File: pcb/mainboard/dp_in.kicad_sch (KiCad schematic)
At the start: 38 parts, among them J602 Molex_47272_DP, U601 PTN3460

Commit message: pcb: r0p4
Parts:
- removed J602: Molex_47272_DP, footprints:472720024, symbol symbols:Molex_47272_DP
- removed R601: 0, Resistor_SMD:R_0402_1005Metric, symbol Device:R
- removed R603, R604: 4.7K, Resistor_SMD:R_0402_1005Metric, symbol Device:R
- removed R605, R606: 10K, Resistor_SMD:R_0402_1005Metric, symbol Device:R
- removed R607, R608, R609, R610, R611, R612, R613, R614, R615, R616: 100, Resistor_SMD:R_0402_1005Metric, symbol Device:R
- removed TP601, TP602: TestPoint, TestPoint:TestPoint_Pad_D1.0mm, symbol Connector:TestPoint
- added C616, C617, C619, C620, C621, C622: 100nF, Capacitor_SMD:C_0402_1005Metric, symbol Device:C
- added C618: 10uF, Capacitor_SMD:C_0603_1608Metric, symbol Device:C
- added J601: USB_C_Receptacle, Connector_USB:USB_C_Receptacle_Amphenol_12401548E4-2A, symbol Connector:USB_C_Receptacle
- added U602: TPS2001D, Package_TO_SOT_SMD:SOT-23-5, symbol symbols:TPS2001D
- added U603: USBLC6-2P6, Package_TO_SOT_SMD:SOT-666, symbol Power_Protection:USBLC6-2P6
- added U604: FUSB302BMPX, Package_DFN_QFN:WQFN-14-1EP_2.5x2.5mm_P0.5mm_EP1.45x1.45mm, symbol Interface_USB:FUSB302BMPX
- added U605: CBTL02043A, Package_DFN_QFN:WQFN-20-1EP_2.5x4.5mm_P0.5mm_EP1x2.9mm, symbol Analog_Switch:CBTL02043A
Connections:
- net +3V3: now also C619.1, C620.1, U604.12 (VCONN), U604.13 (VCONN), U604.3 (VDD), U604.4 (VDD), U605.1 (VDD), U605.10 (VDD), U605.6 (VDD); no longer R617.1
- net DP0N: now also U605.7 (A1_P); no longer C602.2
- net DP0P: now also U605.8 (A1_N); no longer C601.2
- net DP1N: now also U605.3 (A0_P); no longer C604.2
- net DP1P: now also U605.4 (A0_N); no longer C603.2
- net DPAUXN: now also C622.2; no longer C606.2
- net DPAUXP: now also C621.2; no longer C605.2
- net GND: now also R617.1, C618.1, C619.2, C620.2, J601.A1 (GND), J601.A12 (GND), J601.B1 (GND), J601.B12 (GND), J601.S1 (SHIELD), U602.2 (GND), U603.2 (GND), U604.15 (GND), U604.8 (GND), U604.9 (GND), U605.11 (GND), U605.20 (GND), U605.21 (GND), U605.5 (GND), U605.9 (SEL)
- net I2C_SCL: now also U604.6 (SCL)
- net I2C_SDA: now also U604.7 (SDA)
- net DP_HPD: now reaches U601.11 (HPDRX)
- net DP_VALID: now reaches U601.26 (BKLTEN)
- net AUXN renamed TX2P
- net TX2P: now also J601.A11 (RX2+)
- net AUXP renamed TX2N
- net TX2N: now also J601.A10 (RX2-)
- net D0N renamed TX1P
- net TX1P: now also J601.B11 (RX1+)
- net D0P renamed TX1N
- net TX1N: now also J601.B10 (RX1-)
- net D1N renamed RX1P
- net RX1P: now also J601.A2 (TX1+)
- net D1P renamed RX1N
- net RX1N: now also J601.A3 (TX1-)
- net DDC_SCL: no longer names the net of U601.29 (DDC_SCL)
- net DDC_SDA: no longer names the net of U601.30 (DDC_SDA)
- net LVDS_EVEN_CKN: no longer names the net of U601.35 (LVSCKE_N)
- net LVDS_EVEN_CKP: no longer names the net of U601.34 (LVSCKE_P)
- net LVDS_EVEN_DN: no longer names the net of U601.32 (LVSDE_P)
- net LVDS_EVEN_DP: no longer names the net of U601.31 (LVSDE_N)
- net LVDS_ODD_DN: no longer names the net of U601.44 (LVSDO_N)
- net LVDS_ODD_DP: no longer names the net of U601.43 (LVSDO_P)
- new net +5V: C618.2, U602.1 (OUT)
- new net CC1: J601.A5 (CC1), U604.10 (CC1), U604.11 (CC1)
- new net CC2: J601.B5 (CC2), U604.1 (CC2), U604.14 (CC2)
- new net RX1NC: C603.2, U605.17 (B1_P)
- new net RX1PC: C604.2, U605.16 (B1_N)
- new net RX2N: C616.1, J601.B3 (TX2-)
- new net RX2NC: C616.2, U605.13 (C1_P)
- new net RX2P: C617.1, J601.B2 (TX2+)
- new net RX2PC: C617.2, U605.12 (C1_N)
- new net SBU1: C621.1, J601.A8 (SBU1)
- new net SBU2: C622.1, J601.B8 (SBU2)
- new net TCPC_INT: U604.5 (INT_N)
- new net TX1NC: C601.2, U605.19 (B0_P)
- new net TX1PC: C602.2, U605.18 (B0_N)
- new net TX2NC: C605.2, U605.15 (C0_P)
- new net TX2PC: C606.2, U605.14 (C0_N)
- new net TYPEC_ORI: U605.2 (XSD)
- new net USB_DN: J601.A7 (D-), J601.B7 (D-), U603.3 (I/O2), U603.4 (I/O2)
- new net USB_DP: J601.A6 (D+), J601.B6 (D+), U603.1 (I/O1), U603.6 (I/O1)
- new net VBUS: J601.A4 (VBUS), J601.A9 (VBUS), J601.B4 (VBUS), J601.B9 (VBUS), U602.4 (~{EN}), U602.5 (IN), U603.5 (VBUS), U604.2 (VBUS)
- no-connect marks 12 -> 18
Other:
- note added: "SBU reverse is handled by PTN3460"
- note removed: "Use PTN3460 reverse polarity"
- company: (none) -> Copyright 2022 Modos / Engineer: Wenting Zhang
- title: (none) -> Caster EPDC
- moved on the sheet: C607, C608, C609, C610, C611, C612, C613, C614, C615, FB601, FB602, R602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

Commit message: pcb: r0p5
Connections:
- net +3V3: no longer U604.12 (VCONN), U604.13 (VCONN)
- net GND: now also U604.12 (VCONN), U604.13 (VCONN)
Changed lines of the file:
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@@
   (junction (at 208.28 134.62) (diameter 0.9144) (color 0 0 0 0)
   )
-  (junction (at 114.3 76.2) (diameter 0) (color 0 0 0 0)
-  )
   (junction (at 195.58 139.7) (diameter 0.9144) (color 0 0 0 0)
   )
@@
   (junction (at 88.9 55.88) (diameter 0) (color 0 0 0 0)
   )
-  (junction (at 114.3 78.74) (diameter 0) (color 0 0 0 0)
-  )
   (junction (at 116.84 76.2) (diameter 0) (color 0 0 0 0)
   )
@@
   )
   (junction (at 208.28 129.54) (diameter 0.9144) (color 0 0 0 0)
+  )
+  (junction (at 111.76 78.74) (diameter 0) (color 0 0 0 0)
   )
   (junction (at 208.28 101.6) (diameter 0.9144) (color 0 0 0 0)
@@
     (stroke (width 0) (type default) (color 0 0 0 0))
   )
-  (wire (pts (xy 114.3 76.2) (xy 114.3 78.74))
-    (stroke (width 0) (type default) (color 0 0 0 0))
-  )
   (wire (pts (xy 63.5 116.84) (xy 63.5 114.3))
     (stroke (width 0) (type default) (color 0 0 0 0))
@@
     (stroke (width 0) (type solid) (color 0 0 0 0))
   )
-  (wire (pts (xy 114.3 76.2) (xy 116.84 76.2))
+  (wire (pts (xy 95.25 76.2) (xy 116.84 76.2))
+    (stroke (width 0) (type default) (color 0 0 0 0))
+  )
+  (wire (pts (xy 106.68 78.74) (xy 111.76 78.74))
     (stroke (width 0) (type default) (color 0 0 0 0))
   )
@@
   (wire (pts (xy 185.42 91.44) (xy 210.82 91.44))
     (stroke (width 0) (type solid) (color 0 0 0 0))
-  )
-  (wire (pts (xy 95.25 76.2) (xy 114.3 76.2))
-    (stroke (width 0) (type default) (color 0 0 0 0))
   )
   (wire (pts (xy 60.96 157.48) (xy 73.66 157.48))
@@
     (pin "2")
   )
+  (symbol (lib_id "power:GND") (at 106.68 78.74 0) (mirror y) (unit 1)
+    (in_bom yes) (on_board yes)
+    (property "Reference" "#PWR0124" (id 0) (at 106.68 85.09 0)
+      (effects (font (size 1.27 1.27)) hide)
+    )
+    (property "Value" "GND" (id 1) (at 106.68 82.55 0))
+    (property "Footprint" "" (id 2) (at 106.68 78.74 0)
+      (effects (font (size 1.27 1.27)) hide)
+    )
+    (property "Datasheet" "" (id 3) (at 106.68 78.74 0)
+      (effects (font (size 1.27 1.27)) hide)
+    )
+    (pin "1")
+  )
   (symbol (lib_id "Device:FerriteBead") (at 166.37 139.7 90) (unit 1)

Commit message: pcb: r0p6
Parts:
- J601: footprint Connector_USB:USB_C_Receptacle_Amphenol_12401548E4-2A -> footprints:USB-306A-B-SU

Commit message: r0p7 wip, check in before switch to kicad 8
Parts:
- removed C601, C602, C603, C604, C605, C606, C610, C611, C612, C613, C614, C615, C616, C617, C619, C620, C621, C622: 100nF, Capacitor_SMD:C_0402_1005Metric, symbol Device:C
- removed C607, C608, C609: 1uF, Capacitor_SMD:C_0402_1005Metric, symbol Device:C
- removed C618: 10uF, Capacitor_SMD:C_0603_1608Metric, symbol Device:C
- removed FB601, FB602: 120, Inductor_SMD:L_0603_1608Metric, symbol Device:FerriteBead
- removed J601: USB_C_Receptacle, footprints:USB-306A-B-SU, symbol Connector:USB_C_Receptacle
- removed R602, R617: 4.7K, Resistor_SMD:R_0402_1005Metric, symbol Device:R
- removed U601: PTN3460, Package_DFN_QFN:QFN-56-1EP_7x7mm_P0.4mm_EP5.6x5.6mm, symbol symbols:PTN3460
- removed U602: TPS2001D, Package_TO_SOT_SMD:SOT-23-5, symbol symbols:TPS2001D
- removed U603: USBLC6-2P6, Package_TO_SOT_SMD:SOT-666, symbol Power_Protection:USBLC6-2P6
- removed U604: FUSB302BMPX, Package_DFN_QFN:WQFN-14-1EP_2.5x2.5mm_P0.5mm_EP1.45x1.45mm, symbol Interface_USB:FUSB302BMPX
- removed U605: CBTL02043A, Package_DFN_QFN:WQFN-20-1EP_2.5x4.5mm_P0.5mm_EP1x2.9mm, symbol Analog_Switch:CBTL02043A
- added C105, C106, C107, C108, C109, C110, C111, C112, C114, C115, C119, C120, C121, C122, C123, C124, C55, C7: 100nF, Capacitor_SMD:C_0402_1005Metric, symbol Device:C
- added C116, C117, C118: 1uF, Capacitor_SMD:C_0402_1005Metric, symbol Device:C
- added D11, D12, D13: RCLAMP0524P, Package_DFN_QFN:Diodes_UDFN-10_1.0x2.5mm_P0.5mm, symbol symbols:RCLAMP0524P
- added FB1, FB2: 120, Inductor_SMD:L_0603_1608Metric, symbol Device:FerriteBead
- added J1: USB_C_Receptacle, footprints:AMPHENOL_10137065-00021LF, symbol Connector:USB_C_Receptacle
- added R1, R2: 4.7K, Resistor_SMD:R_0402_1005Metric, symbol Device:R
- added U16: USBLC6-2P6, Package_TO_SOT_SMD:SOT-666, symbol Power_Protection:USBLC6-2P6
- added U17: FUSB302BMPX, Package_DFN_QFN:WQFN-14-1EP_2.5x2.5mm_P0.5mm_EP1.45x1.45mm, symbol Interface_USB:FUSB302BMPX
- added U18: CBTL02043A, Package_DFN_QFN:WQFN-20-1EP_2.5x4.5mm_P0.5mm_EP1x2.9mm, symbol Analog_Switch:CBTL02043A
- added U19: PTN3460, Package_DFN_QFN:QFN-56-1EP_7x7mm_P0.4mm_EP5.6x5.6mm, symbol symbols:PTN3460
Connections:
- net +3V3: now also C114.1, C115.1, FB1.1, FB2.1, U17.3 (VDD), U17.4 (VDD), U18.1 (VDD), U18.10 (VDD), U18.6 (VDD)
- net CC1: now also D13.2 (IO2), D13.9 (NC3), J1.A5 (CC1), U17.10 (CC1), U17.11 (CC1)
- net CC2: now also D13.1 (IO1), D13.10 (NC4), J1.B5 (CC2), U17.1 (CC2), U17.14 (CC2)
- net DP0N: now also U18.7 (A1_P), U19.5 (DP0_N)
- net DP0P: now also U18.8 (A1_N), U19.4 (DP0_P)
- net DP1N: now also U18.3 (A0_P), U19.8 (DP1_N)
- net DP1P: now also U18.4 (A0_N), U19.7 (DP1_P)
- net DPAUXN: now also C112.2, U19.1 (AUX_N)
- net DPAUXP: now also C111.2, U19.2 (AUX_P)
- net DP_HPD: now also U19.11 (HPDRX)
- net DP_PDN: now also R1.2, U19.10 (PD_N)
- net DP_VALID: now also U19.26 (BKLTEN)
- net GND: now also C114.2, C115.2, C116.2, C117.2, C118.2, C119.2, C120.2, C121.2, C122.2, C123.2, C124.2, D11.3 (GND), D11.8 (GND), D12.3 (GND), D12.8 (GND), D13.3 (GND), D13.8 (GND), J1.A1 (GND), J1.A12 (GND), J1.B1 (GND), J1.B12 (GND), J1.S1 (SHIELD), R1.1, R2.1, U16.2 (GND), U17.12 (VCONN), U17.13 (VCONN), U17.15 (GND), U17.8 (GND), U17.9 (GND), U18.11 (GND), U18.20 (GND), U18.21 (GND), U18.5 (GND), U18.9 (SEL), U19.17 (GNDREG), U19.18 (GNDREG), U19.3 (GND), U19.57 (EP)
- net I2C_SCL: now also U17.6 (SCL), U19.25 (MS_SCL)
- net I2C_SDA: now also U17.7 (SDA), U19.24 (MS_SDA)
- net LVDS_EVEN_AN: now also U19.42 (LVSAE_N)
- net LVDS_EVEN_AP: now also U19.41 (LVSAE_P)
- net LVDS_EVEN_BN: now also U19.40 (LVSBE_N)
- net LVDS_EVEN_BP: now also U19.39 (LVSBE_P)
- net LVDS_EVEN_CN: now also U19.37 (LVSCE_N)
- net LVDS_EVEN_CP: now also U19.36 (LVSCE_P)
- net LVDS_ODD_AN: now also U19.54 (LVSAO_N)
- net LVDS_ODD_AP: now also U19.53 (LVSAO_P)
- net LVDS_ODD_BN: now also U19.52 (LVSBO_N)
- net LVDS_ODD_BP: now also U19.51 (LVSBO_P)
- net LVDS_ODD_CKN: now also U19.47 (LVSCKO_N)
- net LVDS_ODD_CKP: now also U19.46 (LVSCKO_P)
- net LVDS_ODD_CN: now also U19.49 (LVSCO_N)
- net LVDS_ODD_CP: now also U19.48 (LVSCO_P)
- net RX1N: now also C105.1, D11.2 (IO2), D11.9 (NC3), J1.A3 (TX1-)
- net RX1NC: now also C105.2, U18.17 (B1_P)
- net RX1P: now also C106.1, D11.1 (IO1), D11.10 (NC4), J1.A2 (TX1+)
- net RX1PC: now also C106.2, U18.16 (B1_N)
- net RX2N: now also C109.1, D12.2 (IO2), D12.9 (NC3), J1.B3 (TX2-)
- net RX2NC: now also C109.2, U18.13 (C1_P)
- net RX2P: now also C110.1, D12.1 (IO1), D12.10 (NC4), J1.B2 (TX2+)
- net RX2PC: now also C110.2, U18.12 (C1_N)
- net SBU1: now also C111.1, D13.5 (IO4), D13.6 (NC1), J1.A8 (SBU1)
- net SBU2: now also C112.1, D13.4 (IO3), D13.7 (NC2), J1.B8 (SBU2)
- net TCPC_INT: now also U17.5 (INT_N)
- net TX1N: now also C7.1, D11.5 (IO4), D11.6 (NC1), J1.B10 (RX1-)
- net TX1NC: now also C7.2, U18.19 (B0_P)
- net TX1P: now also C55.1, D11.4 (IO3), D11.7 (NC2), J1.B11 (RX1+)
- net TX1PC: now also C55.2, U18.18 (B0_N)
- net TX2N: now also C107.1, D12.5 (IO4), D12.6 (NC1), J1.A10 (RX2-)
- net TX2NC: now also C107.2, U18.15 (C0_P)
- net TX2P: now also C108.1, D12.4 (IO3), D12.7 (NC2), J1.A11 (RX2+)
- net TX2PC: now also C108.2, U18.14 (C0_N)
- net TYPEC_ORI: now also U18.2 (XSD)
- net USB_DN: now also J1.A7 (D-), J1.B7 (D-), U16.3 (I/O2), U16.4 (I/O2)
- net USB_DP: now also J1.A6 (D+), J1.B6 (D+), U16.1 (I/O1), U16.6 (I/O1)
- net VBUS: now also J1.A4 (VBUS), J1.A9 (VBUS), J1.B4 (VBUS), J1.B9 (VBUS), U16.5 (VBUS), U17.2 (VBUS)
- new net: C116.1, C119.1, C122.1, U19.19 (VDD18REG), U19.45 (VDD18), U19.6 (VDD18)
- new net: C118.1, C121.1, C124.1, FB2.2, U19.38 (VDD33), U19.50 (VDD33)
- new net: C117.1, C120.1, C123.1, FB1.2, U19.13 (VDD33), U19.14 (VDD33)
- new net: R2.2, U19.20 (TESTMODE)
- new net DEC_RST: U19.9 (RST_N)
- no-connect marks 18 -> 16
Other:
- note added: "Use AMPHENOL_10137065-00021LF XUNPU TYPEC-324G-ACP24"

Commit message: r0p7 wip
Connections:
- net GND: no longer U18.11 (GND), U18.20 (GND), U18.21 (GND), U18.5 (GND)
- net RX1NC: now also U18.13 (C1_P); no longer U18.17 (B1_P)
- net RX1PC: now also U18.12 (C1_N); no longer U18.16 (B1_N)
- net RX2NC: now also U18.17 (B1_P); no longer U18.13 (C1_P)
- net RX2PC: now also U18.16 (B1_N); no longer U18.12 (C1_N)
- net TX1NC: now also U18.15 (C0_P); no longer U18.19 (B0_P)
- net TX1PC: now also U18.14 (C0_N); no longer U18.18 (B0_N)
- net TX2NC: now also U18.19 (B0_P); no longer U18.15 (C0_P)
- net TX2PC: now also U18.18 (B0_N); no longer U18.14 (C0_N)
- new net: U18.11 (GND), U18.20 (GND), U18.21 (GND), U18.5 (GND)
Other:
- moved on the sheet: C115, C116, C117, C118, C119, C120, C121, C122, C123, C124, FB1, FB2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

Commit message: r0p7 layout done
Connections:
- net CC1: now also D13.4 (IO3), D13.7 (NC2); no longer D13.2 (IO2), D13.9 (NC3)
- net GND: now also U18.11 (GND), U18.2 (XSD), U18.20 (GND), U18.21 (GND), U18.5 (GND), U19.56 (EPS_N); no longer U18.9 (SEL)
- net SBU2: now also D13.2 (IO2), D13.9 (NC3); no longer D13.4 (IO3), D13.7 (NC2)
- net TYPEC_ORI: now also U18.9 (SEL); no longer U18.2 (XSD)
- net +1V8: now reaches C116.1, C119.1, C122.1, U19.45 (VDD18), U19.6 (VDD18)
- net +1V8: no longer U19.19 (VDD18REG)
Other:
- moved on the sheet: C105, C106, C107, C108, C109, C110, C111, C112, C114, C115, C55, C7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

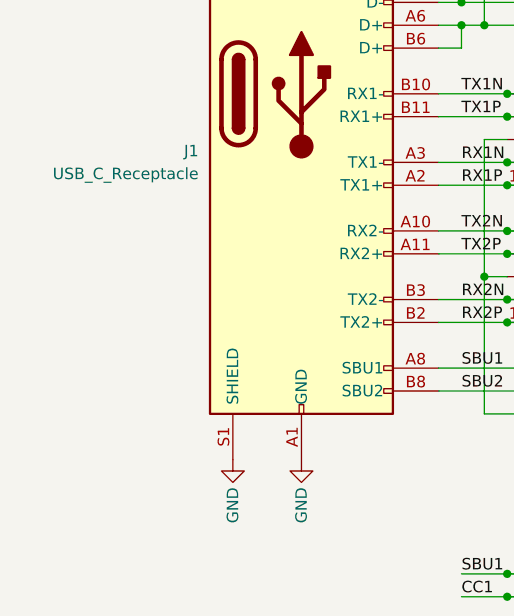
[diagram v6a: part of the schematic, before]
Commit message: Add adapter for ED067KC1/ED113TC1; revise mainboard connector model
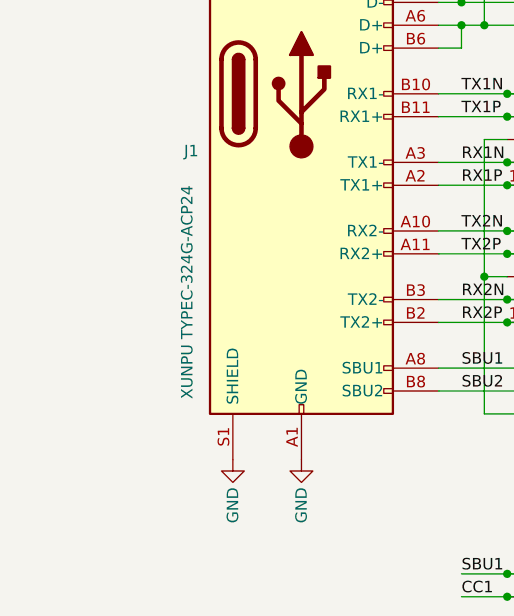
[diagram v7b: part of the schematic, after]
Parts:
- J1: value USB_C_Receptacle -> XUNPU TYPEC-324G-ACP24
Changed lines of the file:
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@@
 			)
 		)
-		(property "Value" "USB_C_Receptacle"
-			(at 29.21 102.87 0)
+		(property "Value" "XUNPU TYPEC-324G-ACP24"
+			(at 27.94 104.14 90)
 			(effects
 				(font

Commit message: Bug fixes and changes for r0p8
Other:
- company: Copyright 2022 Modos / Engineer: Wenting Zhang -> Copyright 2024 Wenting Zhang
- title: Caster EPDC -> Glider
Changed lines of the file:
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@@
 	(paper "A4")
 	(title_block
-		(title "Caster EPDC")
-		(date "2022-07-03")
-		(rev "R0.4")
-		(company "Copyright 2022 Modos / Engineer: Wenting Zhang")
+		(title "Glider")
+		(date "2024-05-09")
+		(rev "R0.8")
+		(company "Copyright 2024 Wenting Zhang")
 	)
 	(junction
